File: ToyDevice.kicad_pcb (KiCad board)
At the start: 2 copper layers, 55 x 45 mm, 45 parts, among them J1 USB_C_Receptacle_USB2.0, J2 Conn_ARM_JTAG_SWD_10, SW1 SW_SPDT, SW2 SW_Push, SW3 SW_Push, SW4 SW_Push, SW5 SW_Push, U1 LP5907MFX-3.3, U2 STM32F070F6Px, Y1 8Mhz Crystal

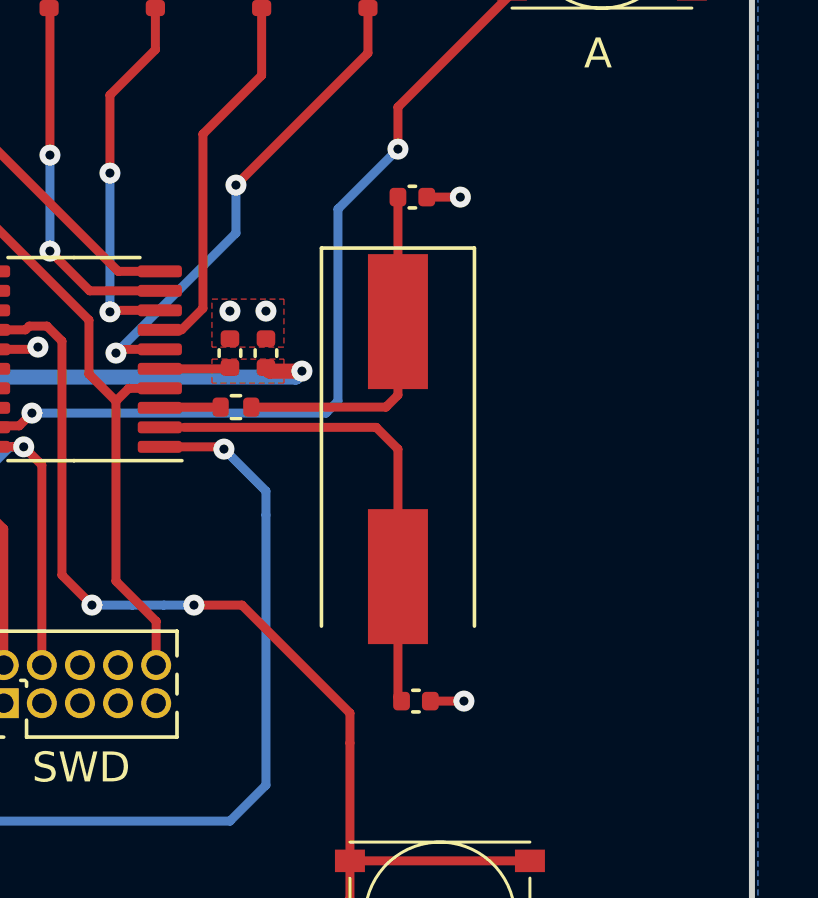
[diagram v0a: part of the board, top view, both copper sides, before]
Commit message: Add all part number
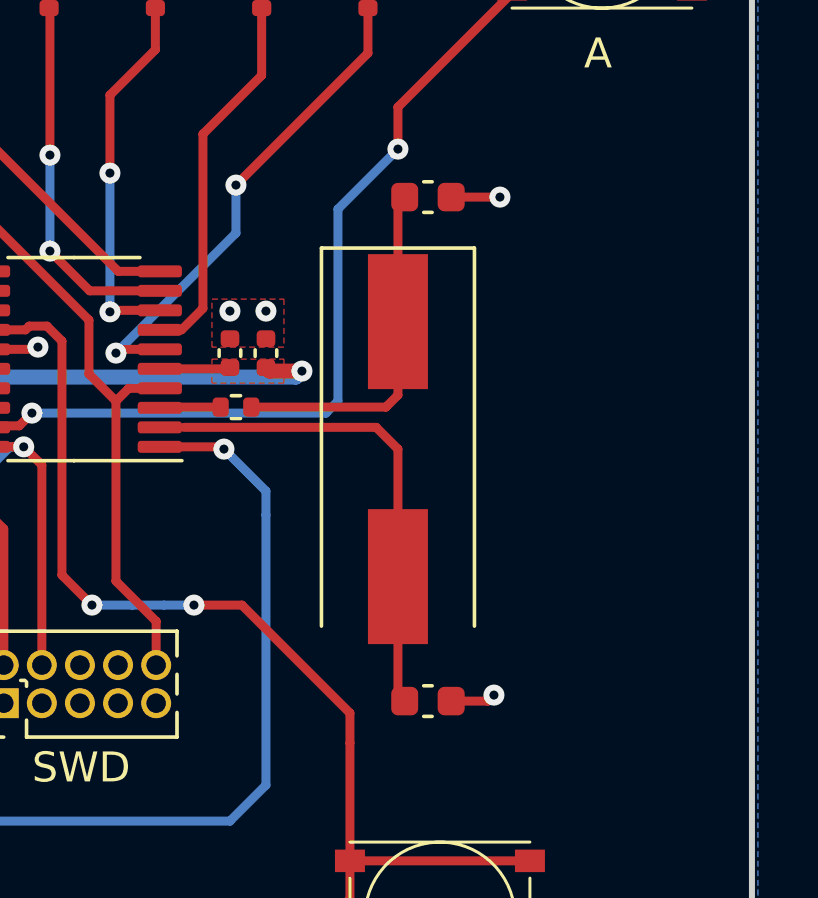
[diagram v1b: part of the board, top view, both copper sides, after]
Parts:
- C3: value 4.7u -> 4u7
- C7, C8: footprint Capacitor_SMD:C_0402_1005Metric -> Capacitor_SMD:C_0603_1608Metric
- R3: value 330R -> 330
- moved C8 0.52 mm to (150.4, 70.6)
- moved C7 0.40 mm to (150.4, 87.4)
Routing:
- net GND: track 32.7 -> 33.6 mm

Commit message: Changed USB-C connector
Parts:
- removed R4: 0R, Resistor_SMD:R_0402_1005Metric
- C7, C8: value 26p -> 15p; footprint Capacitor_SMD:C_0603_1608Metric -> Capacitor_SMD:C_0402_1005Metric
- J1: footprint Connector_USB:USB_C_Receptacle_G-Switch_GT-USB-7010ASV -> Hugo_Custom:SHOU-HAN-TYPE-C-16PFS-2J-H7-45-IPX8
- R10, R11, R12, R13, R3, R6, R7, R8, R9: value 330 -> 330R
- Y1: footprint Crystal:Crystal_SMD_HC49-SD -> Crystal:Crystal_SMD_3225-4Pin_3.2x2.5mm
- moved C8 8.78 mm to (146.0, 78.2), turned to 90 degrees
- moved C7 8.44 mm to (146.0, 80.2), turned to -90 degrees
- moved J1 2.60 mm to (107.2, 83.7)
- moved Y1 0.80 mm to (148.6, 79.0)
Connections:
- C8 pad 2: /RCC_OSC_INT -> /RCC_OSC_OUT
- Y1 pad 1: /RCC_OSC_INT -> /RCC_OSC_OUT
- Y1 pad 2: /RCC_OSC_IN -> GND
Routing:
- net /RCC_OSC_INT: track 11.7 -> 0.00 mm
- net /RCC_OSC_IN: track 15.9 -> 11.4 mm
- net /RCC_OSC_OUT: track 2.04 -> 4.58 mm
- net VBUS: track 21.8 -> 23.2 mm
- net GND: track 33.6 -> 34.5 mm
- net /USB_D+: track 26.6 -> 27.5 mm
- net /USBC_CC2: track 6.09 -> 5.40 mm
- net /USB_D-: track 27.7 -> 28.2 mm

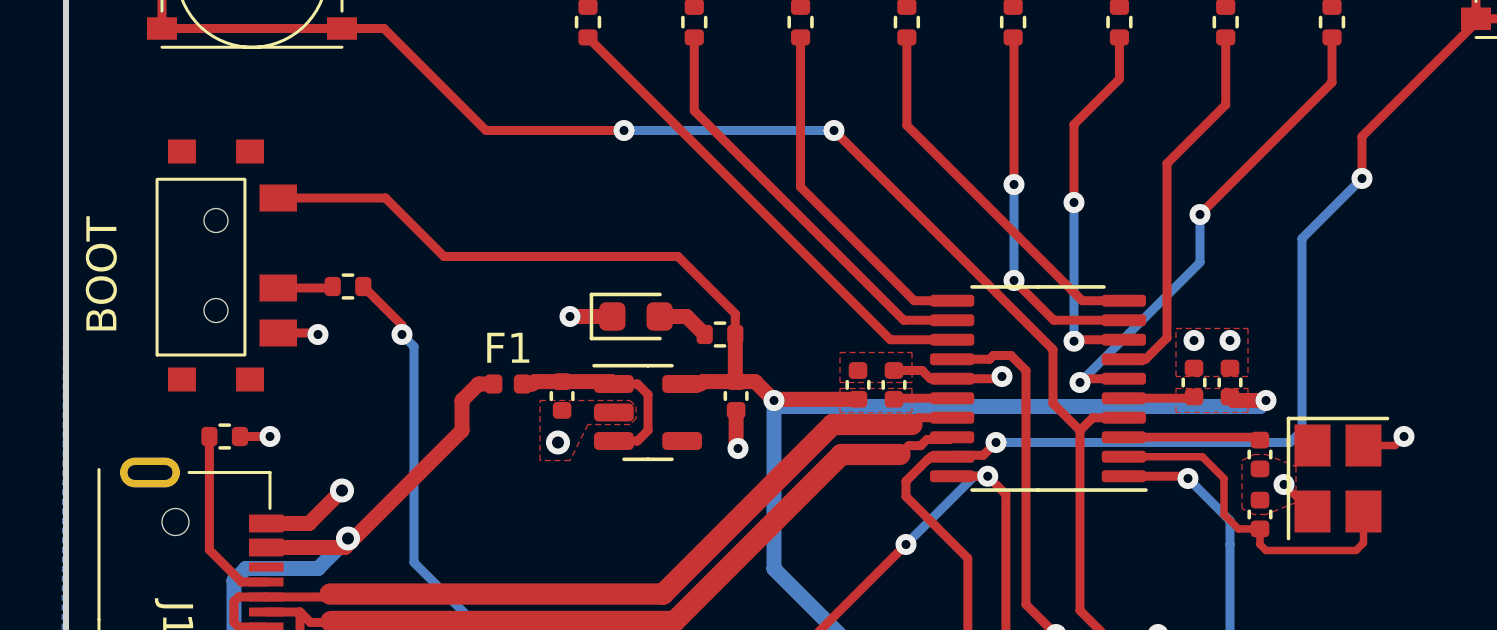
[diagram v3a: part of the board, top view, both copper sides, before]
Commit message: Fix missing connection RCC_OSC_OUT
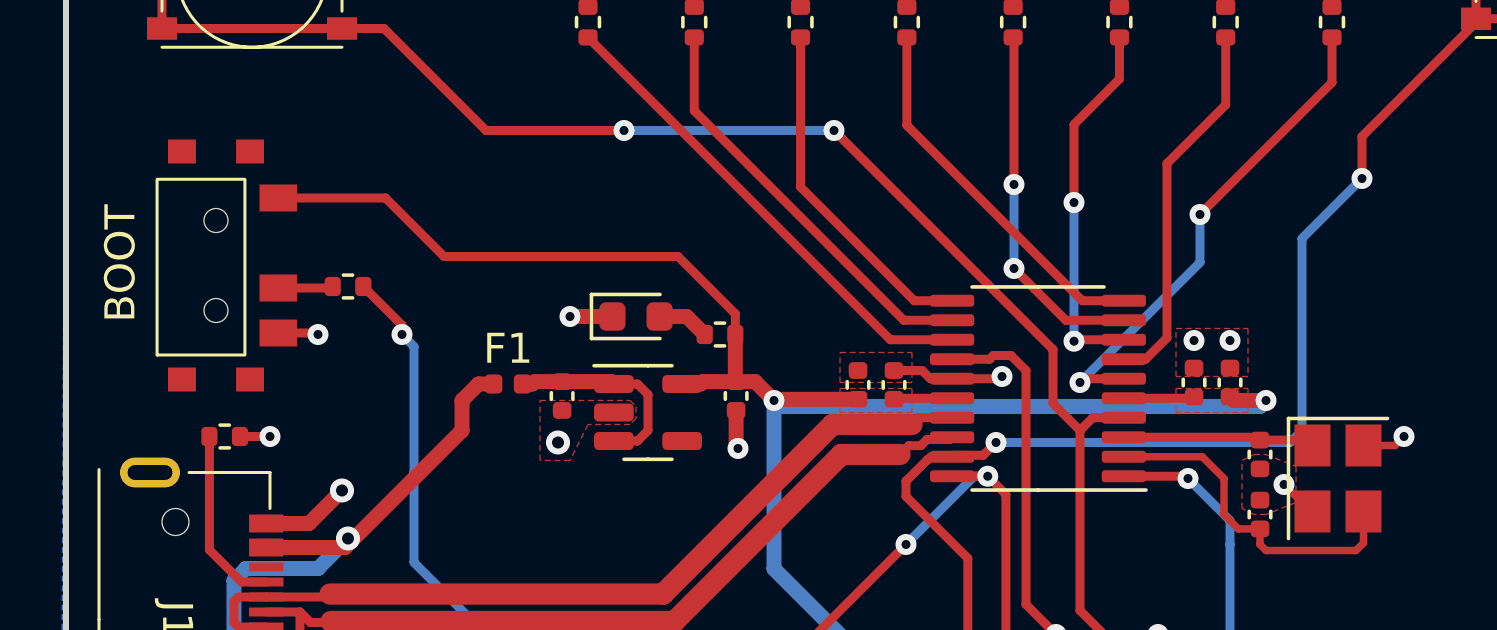
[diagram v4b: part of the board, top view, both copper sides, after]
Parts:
- C7, C8: value 15p -> 16p
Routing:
- net /RCC_OSC_OUT: track 4.58 -> 6.40 mm
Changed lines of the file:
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@@
     )
     (pad_to_mask_clearance 0)
+    (aux_axis_origin 106.2 55.6)
     (pcbplotparams
       (layerselection 0x00010fc_ffffffff)
@@
     (descr "Capacitor SMD 0402 (1005 Metric), square (rectangular) end terminal, IPC_7351 nominal, (Body size source: IPC-SM-782 page 76, https://www.pcb-3d.com/wordpress/wp-content/uploads/ipc-sm-782a_amendment_1_and_2.pdf), generated with kicad-footprint-generator")
     (tags "capacitor")
-    (property "LCSC" "C386131")
-    (property "Mfr Part" "UMK105CG220JV-F")
+    (property "LCSC" "C513591")
+    (property "Mfr Part" "CC0402GRNPO9BN160")
     (property "Sheetfile" "ToyDevice.kicad_sch")
     (property "Sheetname" "")
@@
         (effects (font (size 1 1) (thickness 0.15)))
     )
-    (fp_text value "15p" (at 0 1.16 90) (layer "F.Fab")
+    (fp_text value "16p" (at 0 1.16 90) (layer "F.Fab")
         (effects (font (size 1 1) (thickness 0.15)))
     )
@@
     (descr "Capacitor SMD 0402 (1005 Metric), square (rectangular) end terminal, IPC_7351 nominal, (Body size source: IPC-SM-782 page 76, https://www.pcb-3d.com/wordpress/wp-content/uploads/ipc-sm-782a_amendment_1_and_2.pdf), generated with kicad-footprint-generator")
     (tags "capacitor")
-    (property "LCSC" "C386131")
-    (property "Mfr Part" "UMK105CG220JV-F")
+    (property "LCSC" "C513591")
+    (property "Mfr Part" "CC0402GRNPO9BN160")
     (property "Sheetfile" "ToyDevice.kicad_sch")
     (property "Sheetname" "")
@@
         (effects (font (size 1 1) (thickness 0.15)))
     )
-    (fp_text value "15p" (at 0 1.16 90) (layer "F.Fab")
+    (fp_text value "16p" (at 0 1.16 90) (layer "F.Fab")
         (effects (font (size 1 1) (thickness 0.15)))
     )
@@
     (fp_rect (start -2.98368 -1.964027) (end 2.873173 0.964399)
       (stroke (width 0.1) (type default)) (fill none) (layer "F.SilkS"))
+    (pad "" smd rect (at -3.8 -1.135 90) (size 0.8 0.93) (layers "F.Cu" "F.Paste" "F.Mask")
+      (thermal_bridge_angle 45))
+    (pad "" smd rect (at -3.8 1.135 90) (size 0.8 0.93) (layers "F.Cu" "F.Paste" "F.Mask")
+      (thermal_bridge_angle 45))
     (pad "" np_thru_hole circle (at -1.5 0 90) (size 0.8 0.8) (drill 0.8) (layers "F&B.Cu" "*.Mask"))
     (pad "" np_thru_hole circle (at 1.5 0 90) (size 0.8 0.8) (drill 0.8) (layers "F&B.Cu" "*.Mask"))
+    (pad "" smd rect (at 3.8 -1.135 90) (size 0.8 0.93) (layers "F.Cu" "F.Paste" "F.Mask")
+      (thermal_bridge_angle 45))
+    (pad "" smd rect (at 3.8 1.135 90) (size 0.8 0.93) (layers "F.Cu" "F.Paste" "F.Mask")
+      (thermal_bridge_angle 45))
     (pad "1" smd rect (at -2.25 2.075 90) (size 0.9 1.25) (layers "F.Cu" "F.Paste" "F.Mask")
       (net 1 "GND") (pinfunction "A") (pintype "passive") (thermal_bridge_angle 45))
@@
     (pad "3" smd rect (at 2.25 2.075 90) (size 0.9 1.25) (layers "F.Cu" "F.Paste" "F.Mask")
       (net 2 "+3.3V") (pinfunction "C") (pintype "passive") (thermal_bridge_angle 45))
-    (pad "4" smd rect (at -3.8 -1.135 90) (size 0.8 0.93) (layers "F.Cu" "F.Paste" "F.Mask")
-      (thermal_bridge_angle 45))
-    (pad "4" smd rect (at -3.8 1.135 90) (size 0.8 0.93) (layers "F.Cu" "F.Paste" "F.Mask")
-      (thermal_bridge_angle 45))
-    (pad "4" smd rect (at 3.8 -1.135 90) (size 0.8 0.93) (layers "F.Cu" "F.Paste" "F.Mask")
-      (thermal_bridge_angle 45))
-    (pad "4" smd rect (at 3.8 1.135 90) (size 0.8 0.93) (layers "F.Cu" "F.Paste" "F.Mask")
-      (thermal_bridge_angle 45))
   )
   (footprint "Resistor_SMD:R_0402_1005Metric" (layer "F.Cu")
@@
     (effects (font (size 1 1) (thickness 0.15)) (justify left bottom))
   )
-  (gr_text "BOOT" (at 108 74.2 90) (layer "F.SilkS")
+  (gr_text "BOOT" (at 108.6 73.8 90) (layer "F.SilkS")
     (effects (font (size 1 1) (thickness 0.15)) (justify left bottom))
   )
@@
   (segment (start 141.4625 77.625) (end 145.905 77.625) (width 0.3) (layer "F.Cu") (net 4))
   (segment (start 145.905 77.625) (end 146 77.72) (width 0.3) (layer "F.Cu") (net 4))
+  (segment (start 146 77.72) (end 147.57 77.72) (width 0.3) (layer "F.Cu") (net 4))
+  (segment (start 147.57 77.72) (end 147.75 77.9) (width 0.3) (layer "F.Cu") (net 4))
   (segment (start 108.88 62.08) (end 109.4 62.6) (width 0.3) (layer "F.Cu") (net 5))
   (segment (start 124.8 67.4) (end 120.2 67.4) (width 0.3) (layer "F.Cu") (net 5))
@@
   (via (at 139.8 74.4245) (size 0.7) (drill 0.3) (layers "F.Cu" "B.Cu") (net 33))
   (segment (start 139.8 74.4245) (end 139.8 69.8) (width 0.3) (layer "B.Cu") (net 33))
-  (segment (start 141.4625 73.725) (end 139.125 73.725) (width 0.3) (layer "F.Cu") (net 34))
+  (segment (start 139.525 73.725) (end 141.4625 73.725) (width 0.3) (layer "F.Cu") (net 34))
   (segment (start 137.8 64.326072) (end 137.771428 64.2975) (width 0.3) (layer "F.Cu") (net 34))
   (segment (start 137.8 69.2) (end 137.8 64.326072) (width 0.3) (layer "F.Cu") (net 34))
-  (segment (start 139.125 73.725) (end 137.8 72.4) (width 0.3) (layer "F.Cu") (net 34))
-  (via (at 137.8 72.4) (size 0.7) (drill 0.3) (layers "F.Cu" "B.Cu") (net 34))
+  (segment (start 137.8 72) (end 139.525 73.725) (width 0.3) (layer "F.Cu") (net 34))
+  (via (at 137.8 72) (size 0.7) (drill 0.3) (layers "F.Cu" "B.Cu") (net 34))
   (via (at 137.8 69.2) (size 0.7) (drill 0.3) (layers "F.Cu" "B.Cu") (net 34))
-  (segment (start 137.8 72.4) (end 137.8 69.2) (width 0.3) (layer "B.Cu") (net 34))
+  (segment (start 137.8 72) (end 137.8 69.2) (width 0.3) (layer "B.Cu") (net 34))
   (segment (start 140.075 73.075) (end 141.4625 73.075) (width 0.3) (layer "F.Cu") (net 35))
   (segment (start 134.228571 64.2975) (end 134.228571 67.228571) (width 0.3) (layer "F.Cu") (net 35))
